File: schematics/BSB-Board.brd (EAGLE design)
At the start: 29.7 x 53.3 mm, 23 parts, among them Q1 BC 547A, Q11 BC 557A, Q12 BC 547A, U1 4N25, U2 4N25

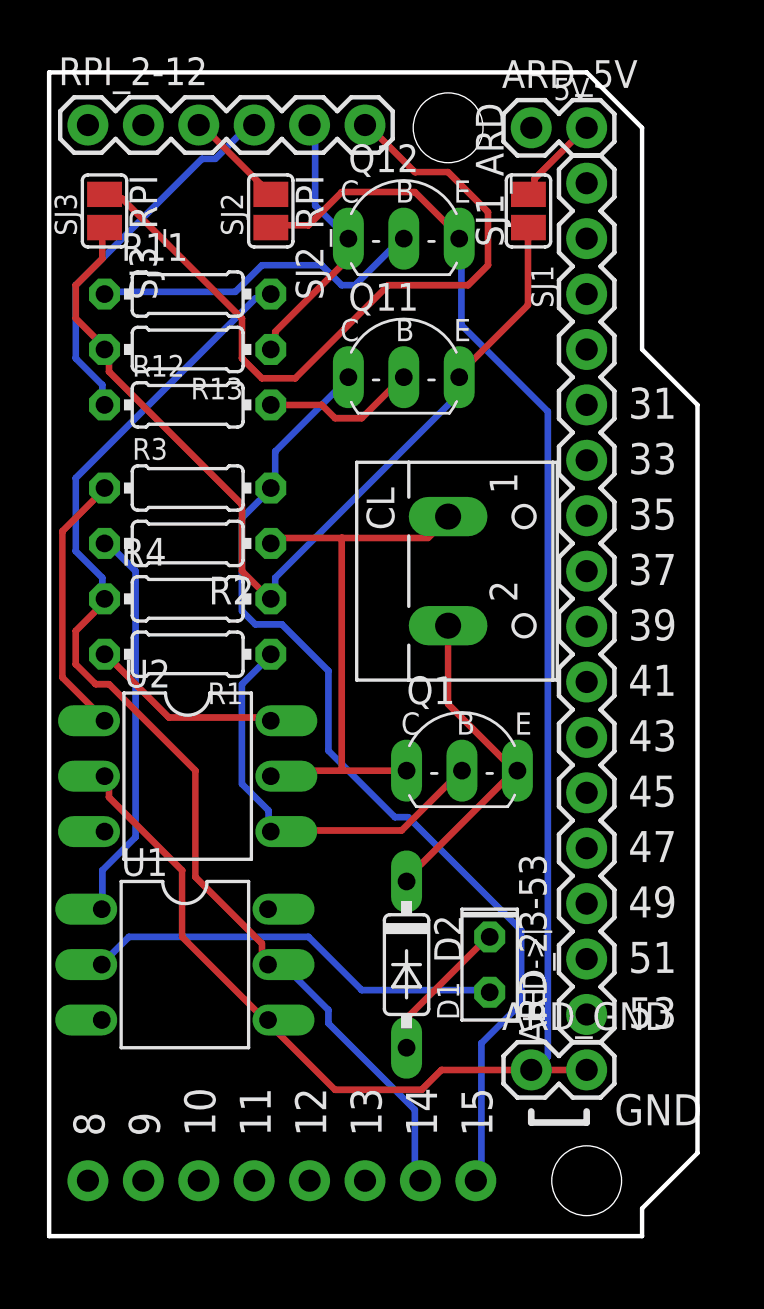
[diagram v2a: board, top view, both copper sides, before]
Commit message: Minor alignment of RX OC
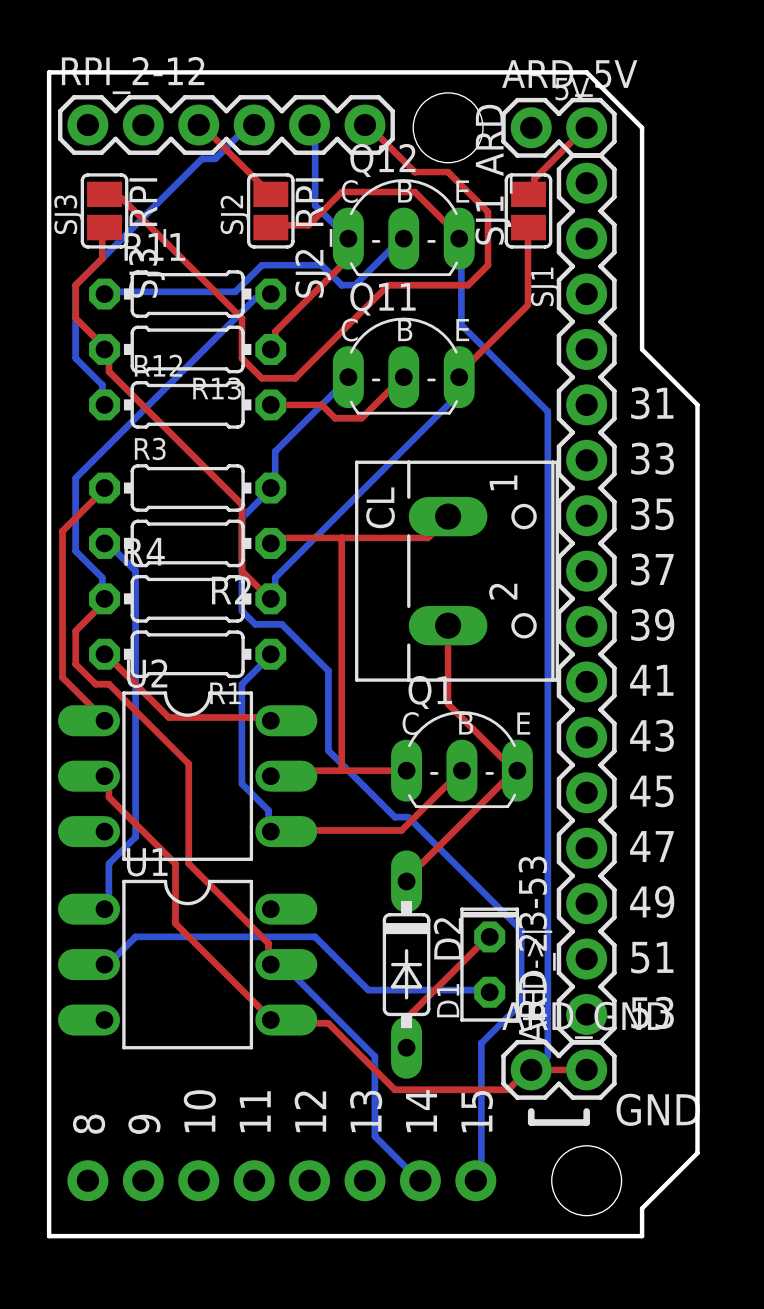
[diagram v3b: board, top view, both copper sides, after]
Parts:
- moved U1 0.13 mm to (6.35, 12.4)
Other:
- board text added: "Schematics by G.Schumacher / J.Loehnert Board layout (C) by Frederik Holst"
- board text removed: "Schematics by G.Schumacher / J.Loehnert Board layout by Frederik Holst"
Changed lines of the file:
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@@
 Raspi: connect SJ2 (GND) and S3 (3.3V)</text>
 <text x="28.956" y="38.608" size="1.016" layer="22" rot="MR270">Schematics by G.Schumacher / J.Loehnert
-Board layout by Frederik Holst</text>
+Board layout (C) by Frederik Holst</text>
 <wire x1="0.381" y1="49.022" x2="20.701" y2="49.022" width="0.254" layer="27" style="shortdash"/>
 <wire x1="20.701" y1="49.022" x2="20.701" y2="35.814" width="0.254" layer="27" style="shortdash"/>
@@
 <element name="ARD_GND" library="SparkFun-Connectors" package="1X02" value="" x="22.098" y="7.62"/>
 <element name="ARD_5V" library="SparkFun-Connectors" package="1X02" value="" x="22.098" y="50.8"/>
-<element name="U1" library="optocoupler" package="DIL06" value="4N25" x="6.223" y="12.446" rot="R270">
-<attribute name="MF" value="" x="6.223" y="12.446" size="1.778" layer="27" rot="R270" display="off"/>
-<attribute name="MPN" value="4N25-M" x="6.223" y="12.446" size="1.778" layer="27" rot="R270" display="off"/>
-<attribute name="OC_FARNELL" value="1021349" x="6.223" y="12.446" size="1.778" layer="27" rot="R270" display="off"/>
-<attribute name="OC_NEWARK" value="98K9084" x="6.223" y="12.446" size="1.778" layer="27" rot="R270" display="off"/>
+<element name="U1" library="optocoupler" package="DIL06" value="4N25" x="6.35" y="12.446" rot="R270">
+<attribute name="MF" value="" x="6.35" y="12.446" size="1.778" layer="27" rot="R270" display="off"/>
+<attribute name="MPN" value="4N25-M" x="6.35" y="12.446" size="1.778" layer="27" rot="R270" display="off"/>
+<attribute name="OC_FARNELL" value="1021349" x="6.35" y="12.446" size="1.778" layer="27" rot="R270" display="off"/>
+<attribute name="OC_NEWARK" value="98K9084" x="6.35" y="12.446" size="1.778" layer="27" rot="R270" display="off"/>
 </element>
 <element name="U2" library="optocoupler" package="DIL06" value="4N25" x="6.35" y="21.082" rot="R270">
@@
 <signal name="A14-RXD-ARD">
 <contactref element="U1" pad="5"/>
-<wire x1="9.7536" y1="13.4112" x2="9.7536" y2="12.4968" width="0.3048" layer="1"/>
-<wire x1="6.7056" y1="16.4592" x2="9.7536" y2="13.4112" width="0.3048" layer="1"/>
-<wire x1="6.7056" y1="21.336" x2="6.7056" y2="16.4592" width="0.3048" layer="1"/>
-<wire x1="2.7432" y1="25.2984" x2="6.7056" y2="21.336" width="0.3048" layer="1"/>
-<wire x1="2.1336" y1="25.2984" x2="2.7432" y2="25.2984" width="0.3048" layer="1"/>
-<wire x1="1.2192" y1="26.2128" x2="2.1336" y2="25.2984" width="0.3048" layer="1"/>
-<wire x1="1.2192" y1="27.7368" x2="1.2192" y2="26.2128" width="0.3048" layer="1"/>
-<wire x1="2.4384" y1="28.956" x2="1.2192" y2="27.7368" width="0.3048" layer="1"/>
-<wire x1="9.7536" y1="12.4968" x2="10.033" y2="12.446" width="0.3048" layer="1"/>
 <contactref element="R4" pad="1"/>
 <contactref element="R11" pad="2"/>
@@
 <wire x1="2.4384" y1="29.2608" x2="2.54" y2="29.21" width="0.3048" layer="16"/>
 <wire x1="10.0584" y1="42.9768" x2="10.16" y2="43.18" width="0.3048" layer="16"/>
-<wire x1="16.764" y1="5.7912" x2="16.764" y2="2.7432" width="0.3048" layer="16"/>
-<wire x1="12.8016" y1="9.7536" x2="16.764" y2="5.7912" width="0.3048" layer="16"/>
-<wire x1="12.8016" y1="10.3632" x2="12.8016" y2="9.7536" width="0.3048" layer="16"/>
-<wire x1="10.9728" y1="12.192" x2="12.8016" y2="10.3632" width="0.3048" layer="16"/>
-<wire x1="10.0584" y1="12.192" x2="10.9728" y2="12.192" width="0.3048" layer="16"/>
+<wire x1="10.9728" y1="12.192" x2="10.3632" y2="12.192" width="0.3048" layer="16"/>
+<wire x1="14.9352" y1="8.2296" x2="10.9728" y2="12.192" width="0.3048" layer="16"/>
+<wire x1="14.9352" y1="4.572" x2="14.9352" y2="8.2296" width="0.3048" layer="16"/>
+<wire x1="16.764" y1="2.7432" x2="14.9352" y2="4.572" width="0.3048" layer="16"/>
+<wire x1="10.3632" y1="12.192" x2="10.16" y2="12.446" width="0.3048" layer="16"/>
 <wire x1="16.764" y1="2.7432" x2="17.018" y2="2.54" width="0.3048" layer="16"/>
-<wire x1="10.0584" y1="12.192" x2="10.033" y2="12.446" width="0.3048" layer="16"/>
+<wire x1="10.0584" y1="13.4112" x2="10.0584" y2="12.4968" width="0.3048" layer="1"/>
+<wire x1="6.4008" y1="17.0688" x2="10.0584" y2="13.4112" width="0.3048" layer="1"/>
+<wire x1="6.4008" y1="21.6408" x2="6.4008" y2="17.0688" width="0.3048" layer="1"/>
+<wire x1="2.7432" y1="25.2984" x2="6.4008" y2="21.6408" width="0.3048" layer="1"/>
+<wire x1="2.1336" y1="25.2984" x2="2.7432" y2="25.2984" width="0.3048" layer="1"/>
+<wire x1="1.2192" y1="26.2128" x2="2.1336" y2="25.2984" width="0.3048" layer="1"/>
+<wire x1="1.2192" y1="27.7368" x2="1.2192" y2="26.2128" width="0.3048" layer="1"/>
+<wire x1="2.4384" y1="28.956" x2="1.2192" y2="27.7368" width="0.3048" layer="1"/>
+<wire x1="10.0584" y1="12.4968" x2="10.16" y2="12.446" width="0.3048" layer="1"/>
 <wire x1="2.4384" y1="28.956" x2="2.54" y2="29.21" width="0.3048" layer="1"/>
 </signal>
@@
 <contactref element="U1" pad="1"/>
 <contactref element="R2" pad="2"/>
-<wire x1="2.4384" y1="16.764" x2="2.4384" y2="15.24" width="0.3048" layer="16"/>
-<wire x1="3.9624" y1="18.288" x2="2.4384" y2="16.764" width="0.3048" layer="16"/>
+<wire x1="2.7432" y1="17.0688" x2="2.7432" y2="15.24" width="0.3048" layer="16"/>
+<wire x1="3.9624" y1="18.288" x2="2.7432" y2="17.0688" width="0.3048" layer="16"/>
 <wire x1="3.9624" y1="30.48" x2="3.9624" y2="18.288" width="0.3048" layer="16"/>
 <wire x1="2.7432" y1="31.6992" x2="3.9624" y2="30.48" width="0.3048" layer="16"/>
-<wire x1="2.4384" y1="15.24" x2="2.413" y2="14.986" width="0.3048" layer="16"/>
+<wire x1="2.7432" y1="15.24" x2="2.54" y2="14.986" width="0.3048" layer="16"/>
 <wire x1="2.7432" y1="31.6992" x2="2.54" y2="31.75" width="0.3048" layer="16"/>
 </signal>
@@
 <contactref element="U1" pad="2"/>
 <contactref element="D1" pad="A"/>
-<wire x1="14.3256" y1="11.2776" x2="20.1168" y2="11.2776" width="0.3048" layer="16"/>
-<wire x1="11.8872" y1="13.716" x2="14.3256" y2="11.2776" width="0.3048" layer="16"/>
-<wire x1="3.6576" y1="13.716" x2="11.8872" y2="13.716" width="0.3048" layer="16"/>
-<wire x1="2.4384" y1="12.4968" x2="3.6576" y2="13.716" width="0.3048" layer="16"/>
+<wire x1="14.6304" y1="11.2776" x2="20.1168" y2="11.2776" width="0.3048" layer="16"/>
+<wire x1="12.192" y1="13.716" x2="14.6304" y2="11.2776" width="0.3048" layer="16"/>
+<wire x1="3.9624" y1="13.716" x2="12.192" y2="13.716" width="0.3048" layer="16"/>
+<wire x1="2.7432" y1="12.4968" x2="3.9624" y2="13.716" width="0.3048" layer="16"/>
 <wire x1="20.1168" y1="11.2776" x2="20.193" y2="11.176" width="0.3048" layer="16"/>
-<wire x1="2.4384" y1="12.4968" x2="2.413" y2="12.446" width="0.3048" layer="16"/>
+<wire x1="2.7432" y1="12.4968" x2="2.54" y2="12.446" width="0.3048" layer="16"/>
 </signal>
 <signal name="N$3">
@@
 <contactref element="Q12" pad="E"/>
 <contactref element="SJ2_RPI" pad="2"/>
-<wire x1="2.7432" y1="20.1168" x2="2.7432" y2="21.0312" width="0.3048" layer="1"/>
-<wire x1="6.096" y1="16.764" x2="2.7432" y2="20.1168" width="0.3048" layer="1"/>
-<wire x1="6.096" y1="13.716" x2="6.096" y2="16.764" width="0.3048" layer="1"/>
-<wire x1="9.7536" y1="10.0584" x2="6.096" y2="13.716" width="0.3048" layer="1"/>
-<wire x1="2.7432" y1="21.0312" x2="2.54" y2="21.082" width="0.3048" layer="1"/>
-<wire x1="9.7536" y1="10.0584" x2="10.033" y2="9.906" width="0.3048" layer="1"/>
 <wire x1="11.8872" y1="46.3296" x2="10.3632" y2="46.3296" width="0.3048" layer="1"/>
 <wire x1="13.4112" y1="47.8536" x2="11.8872" y2="46.3296" width="0.3048" layer="1"/>
@@
 <wire x1="18.8976" y1="45.72" x2="18.796" y2="45.72" width="0.3048" layer="1"/>
 <wire x1="24.638" y1="7.62" x2="22.098" y2="7.62" width="0.3048" layer="1"/>
-<wire x1="17.9832" y1="7.62" x2="22.098" y2="7.62" width="0.3048" layer="1"/>
-<wire x1="17.0688" y1="6.7056" x2="17.9832" y2="7.62" width="0.3048" layer="1"/>
-<wire x1="13.1064" y1="6.7056" x2="17.0688" y2="6.7056" width="0.3048" layer="1"/>
-<wire x1="10.0584" y1="9.7536" x2="13.1064" y2="6.7056" width="0.3048" layer="1"/>
-<wire x1="10.0584" y1="9.7536" x2="10.033" y2="9.906" width="0.3048" layer="1"/>
 <wire x1="18.8976" y1="41.7576" x2="18.8976" y2="45.72" width="0.3048" layer="16"/>
 <wire x1="22.86" y1="37.7952" x2="18.8976" y2="41.7576" width="0.3048" layer="16"/>
@@
 <wire x1="18.8976" y1="45.72" x2="18.796" y2="45.72" width="0.3048" layer="16"/>
 <wire x1="22.2504" y1="7.62" x2="22.098" y2="7.62" width="0.3048" layer="16"/>
+<wire x1="2.7432" y1="20.1168" x2="2.7432" y2="21.0312" width="0.3048" layer="1"/>
+<wire x1="5.7912" y1="17.0688" x2="2.7432" y2="20.1168" width="0.3048" layer="1"/>
+<wire x1="5.7912" y1="14.3256" x2="5.7912" y2="17.0688" width="0.3048" layer="1"/>
+<wire x1="10.0584" y1="10.0584" x2="5.7912" y2="14.3256" width="0.3048" layer="1"/>
+<wire x1="2.7432" y1="21.0312" x2="2.54" y2="21.082" width="0.3048" layer="1"/>
+<wire x1="10.0584" y1="10.0584" x2="10.16" y2="9.906" width="0.3048" layer="1"/>
+<wire x1="12.8016" y1="9.7536" x2="10.3632" y2="9.7536" width="0.3048" layer="1"/>
+<wire x1="15.8496" y1="6.7056" x2="12.8016" y2="9.7536" width="0.3048" layer="1"/>
+<wire x1="21.0312" y1="6.7056" x2="15.8496" y2="6.7056" width="0.3048" layer="1"/>
+<wire x1="21.9456" y1="7.62" x2="21.0312" y2="6.7056" width="0.3048" layer="1"/>
+<wire x1="10.3632" y1="9.7536" x2="10.16" y2="9.906" width="0.3048" layer="1"/>
+<wire x1="21.9456" y1="7.62" x2="22.098" y2="7.62" width="0.3048" layer="1"/>
 </signal>
 <signal name="GPIO15-RXD-PI">
